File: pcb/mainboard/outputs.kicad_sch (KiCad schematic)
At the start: 71 parts, among them U38 ISL24021IRT065Z-T7A‎, U39 ISL24021IRT065Z-T7A‎, U40 ISL24021IRT065Z-T7A‎, U41 ISL24021IRT065Z-T7A‎, U42 DAC60508, U43 ISL24021IRT065Z-T7A‎, U44 ISL24021IRT065Z-T7A‎, U45 ISL24021IRT065Z-T7A‎, U46 ISL24021IRT065Z-T7A‎, U47 74LVC1T45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

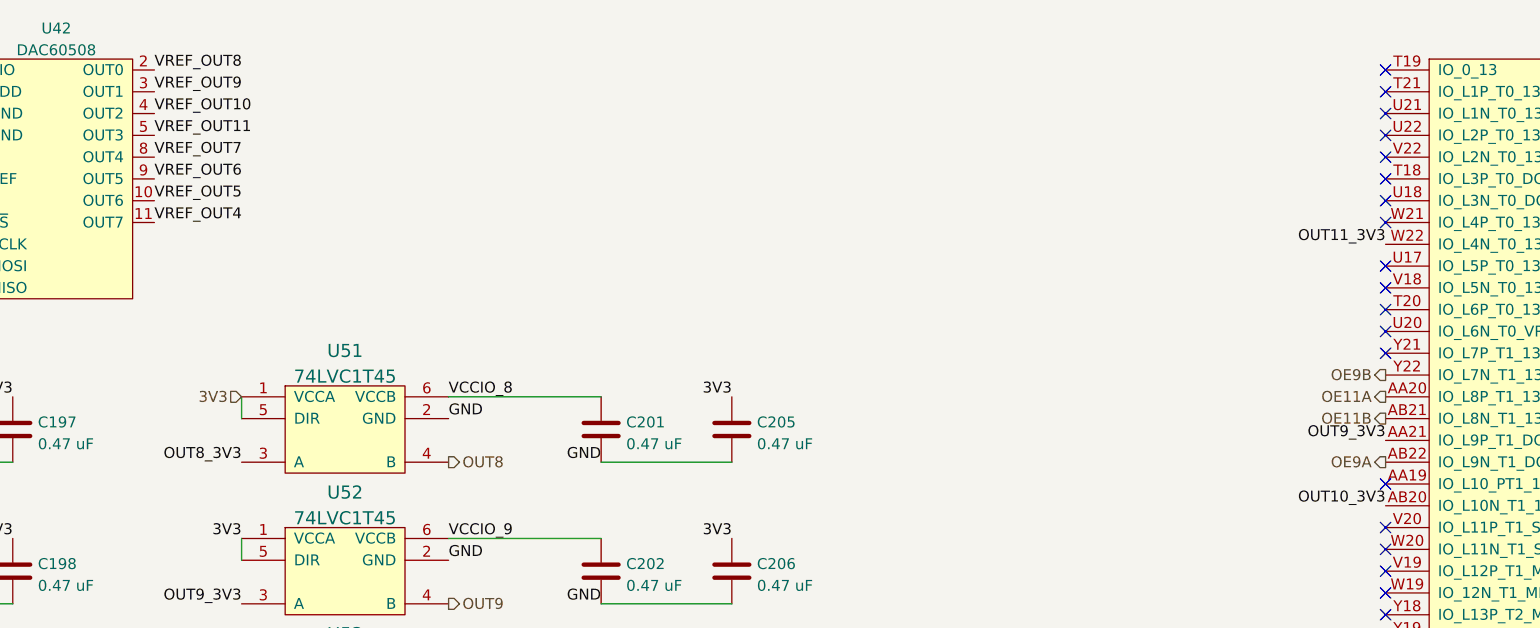
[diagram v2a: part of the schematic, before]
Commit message: Continued layout, started plane fills. Everything routed except 1V8 regulator
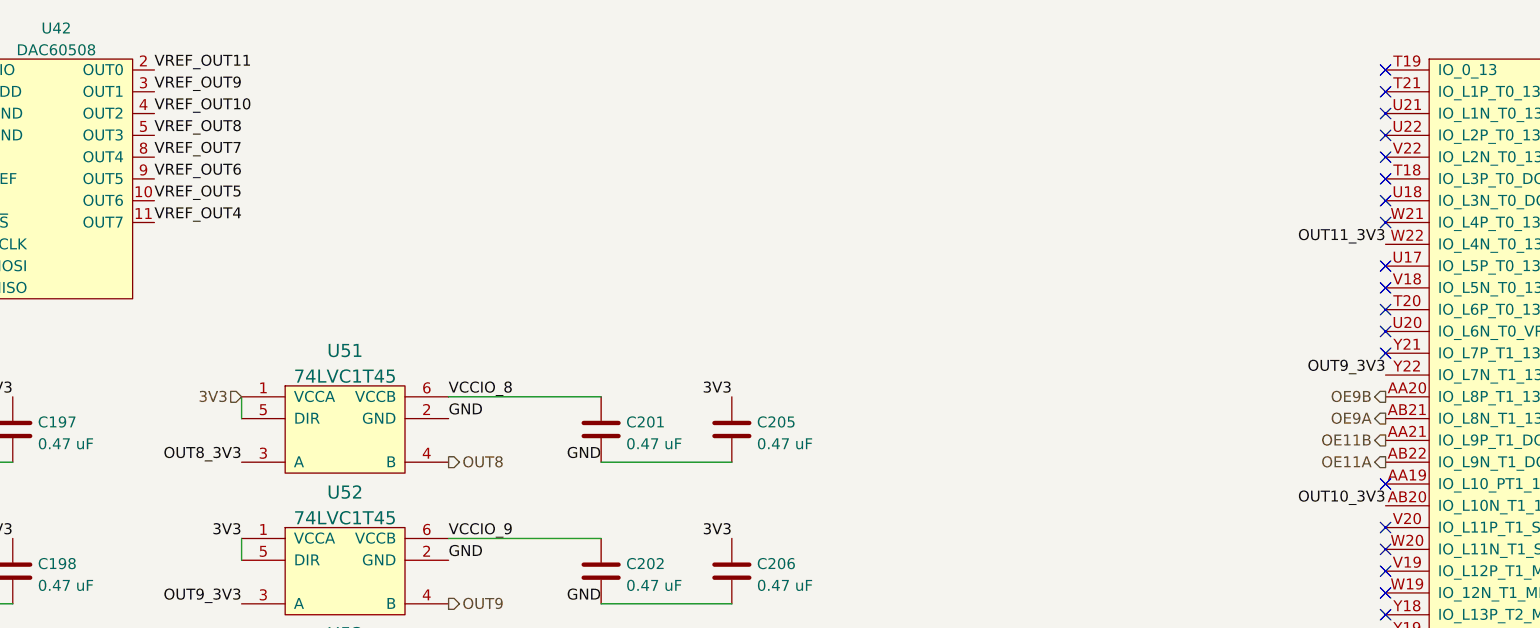
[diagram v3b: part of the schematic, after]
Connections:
- net OE11A: now also U8.AB22 (IO_L9N_T1_DQS_13); no longer U8.AA20 (IO_L8P_T1_13)
- net OE11B: now also U8.AA21 (IO_L9P_T1_DQS_13); no longer U8.AB21 (IO_L8N_T1_13)
- net OE9A: now also U8.AB21 (IO_L8N_T1_13); no longer U8.AB22 (IO_L9N_T1_DQS_13)
- net OE9B: now also U8.AA20 (IO_L8P_T1_13); no longer U8.Y22 (IO_L7N_T1_13)
- net OUT9_3V3: now also U8.Y22 (IO_L7N_T1_13); no longer U8.AA21 (IO_L9P_T1_DQS_13)
- net VREF_OUT11: now also U42.2 (OUT0); no longer U42.5 (OUT3)
- net VREF_OUT8: now also U42.5 (OUT3); no longer U42.2 (OUT0)
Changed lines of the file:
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@@
   (title_block
     (title "Trigger Crossbar")
-    (date "2023-12-22")
+    (date "2023-12-25")
     (rev "0.1")
     (company "Antikernel Labs")
@@
     (effects (font (size 1.27 1.27)) (justify right bottom))
   )
-  (label "OUT9_3V3" (at 349.25 69.85 180)
+  (label "OUT9_3V3" (at 349.25 62.23 180)
     (effects (font (size 1.27 1.27)) (justify right bottom))
   )
@@
     (effects (font (size 1.27 1.27)) (justify left bottom))
   )
-  (label "VREF_OUT8" (at 205.74 26.67 0)
+  (label "VREF_OUT8" (at 205.74 34.29 0)
     (effects (font (size 1.27 1.27)) (justify left bottom))
   )
@@
     (effects (font (size 1.27 1.27)) (justify right bottom))
   )
-  (label "VREF_OUT11" (at 205.74 34.29 0)
+  (label "VREF_OUT11" (at 205.74 26.67 0)
     (effects (font (size 1.27 1.27)) (justify left bottom))
   )
@@
     (effects (font (size 1.27 1.27)) (justify left))
   )
-  (hierarchical_label "OE9A" (shape output) (at 349.25 72.39 180)
+  (hierarchical_label "OE9A" (shape output) (at 349.25 67.31 180)
     (effects (font (size 1.27 1.27)) (justify right))
   )
@@
     (effects (font (size 1.27 1.27)) (justify right))
   )
-  (hierarchical_label "OE9B" (shape output) (at 349.25 62.23 180)
-    (effects (font (size 1.27 1.27)) (justify right))
-  )
-  (hierarchical_label "OE11B" (shape output) (at 349.25 67.31 180)
+  (hierarchical_label "OE9B" (shape output) (at 349.25 64.77 180)
+    (effects (font (size 1.27 1.27)) (justify right))
+  )
+  (hierarchical_label "OE11B" (shape output) (at 349.25 69.85 180)
     (effects (font (size 1.27 1.27)) (justify right))
   )
@@
     (effects (font (size 1.27 1.27)) (justify left))
   )
-  (hierarchical_label "OE11A" (shape output) (at 349.25 64.77 180)
-    (effects (font (size 1.27 1.27)) (justify right))
-  )
+  (hierarchical_label "OE11A" (shape output) (at 349.25 72.39 180)
+    (effects (font (size 1.27 1.27)) (justify right))
+  )
